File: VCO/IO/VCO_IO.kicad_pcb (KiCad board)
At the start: 2 copper layers, 43.2 x 111.8 mm, 31 parts, among them J1 Saw, J10 Sync, J11 LIN, J12 IO, J2 CV1, J3 CV2, J4 CV3, J5 Pulse, J6 Ramp, J7 Tri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

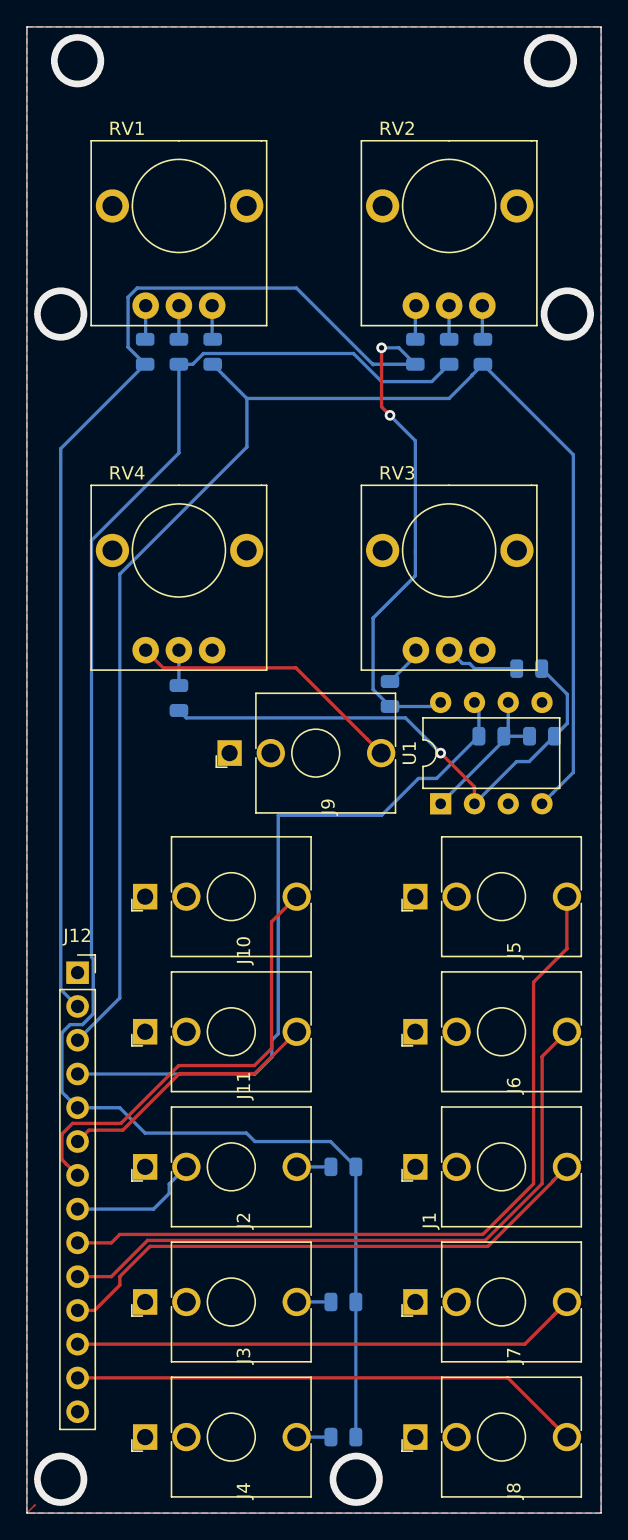
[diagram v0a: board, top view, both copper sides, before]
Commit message: Fix minor issues with VCO board
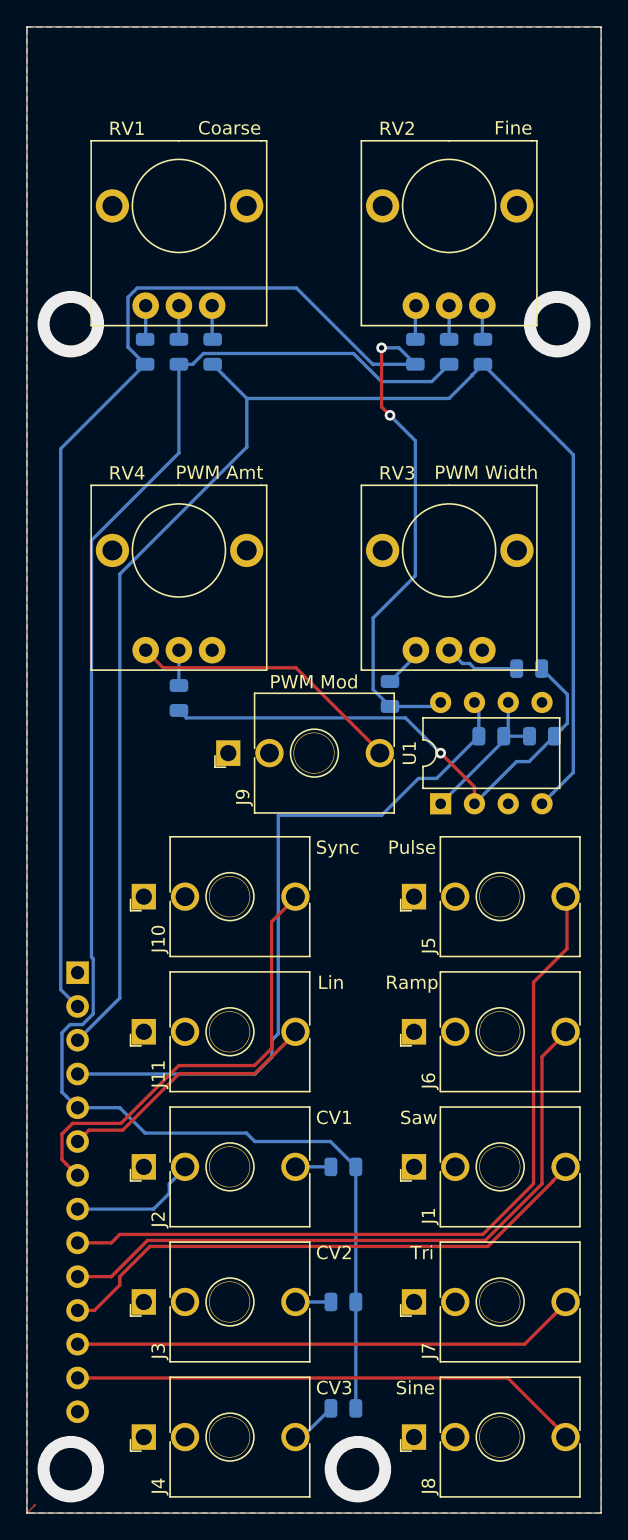
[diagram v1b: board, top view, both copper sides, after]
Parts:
- added REF**: OSHW-Logo2_7.3x6mm_SilkScreen, Symbol:OSHW-Logo2_7.3x6mm_SilkScreen, B.Cu at (77.2, 52.8)
- J12: moved to B.Cu
- moved R7 2.16 mm to (91.1, 152.1)
- turned J12 to 180 degrees
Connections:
- RV1 pad : (no net) -> GNDREF
- RV2 pad : (no net) -> GNDREF
- RV3 pad : (no net) -> GNDREF
- RV4 pad : (no net) -> GNDREF
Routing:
- net /CV: track 125.9 -> 123.7 mm
- net Net-(J4-PadT): track 2.57 -> 3.46 mm
- net GNDREF: vias 6 -> 4
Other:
- board text added: "CV1"
- board text added: "CV2"
- board text added: "CV3"
- board text added: "Coarse"
- board text added: "Fine"
- board text added: "Lin"
- board text added: "PWM Amt"
- board text added: "PWM Mod"
- board text added: "PWM Width"
- board text added: "Pulse"
- board text added: "Ramp"
- board text added: "Saw"
- board text added: "Sine"
- board text added: "Sync"
- board text added: "Tri"
- board text added: "VCO IO Board Rev 1"
- board text added: "WH"

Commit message: Bunch of bug fixes and tweaks
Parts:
- added H1: Top_MH1, Eurorack:eurorack_mounting_hole, F.Cu at (70.6, 70.6)
- added H2: Bottom_MH1, Eurorack:eurorack_mounting_hole, F.Cu at (70.6, 156.7)
- added H3: Top_MH2, Eurorack:eurorack_mounting_hole, F.Cu at (107.2, 70.6)
- added H4: Bottom_MH2, Eurorack:eurorack_mounting_hole, F.Cu at (92.2, 156.7)
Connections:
- RV1 pad : GNDREF -> (no net)
- RV2 pad : GNDREF -> (no net)
- RV3 pad : GNDREF -> (no net)
- RV4 pad : GNDREF -> (no net)
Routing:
- net /PWM: track 53.7 -> 50.6 mm
- net GNDREF: vias 4 -> 0

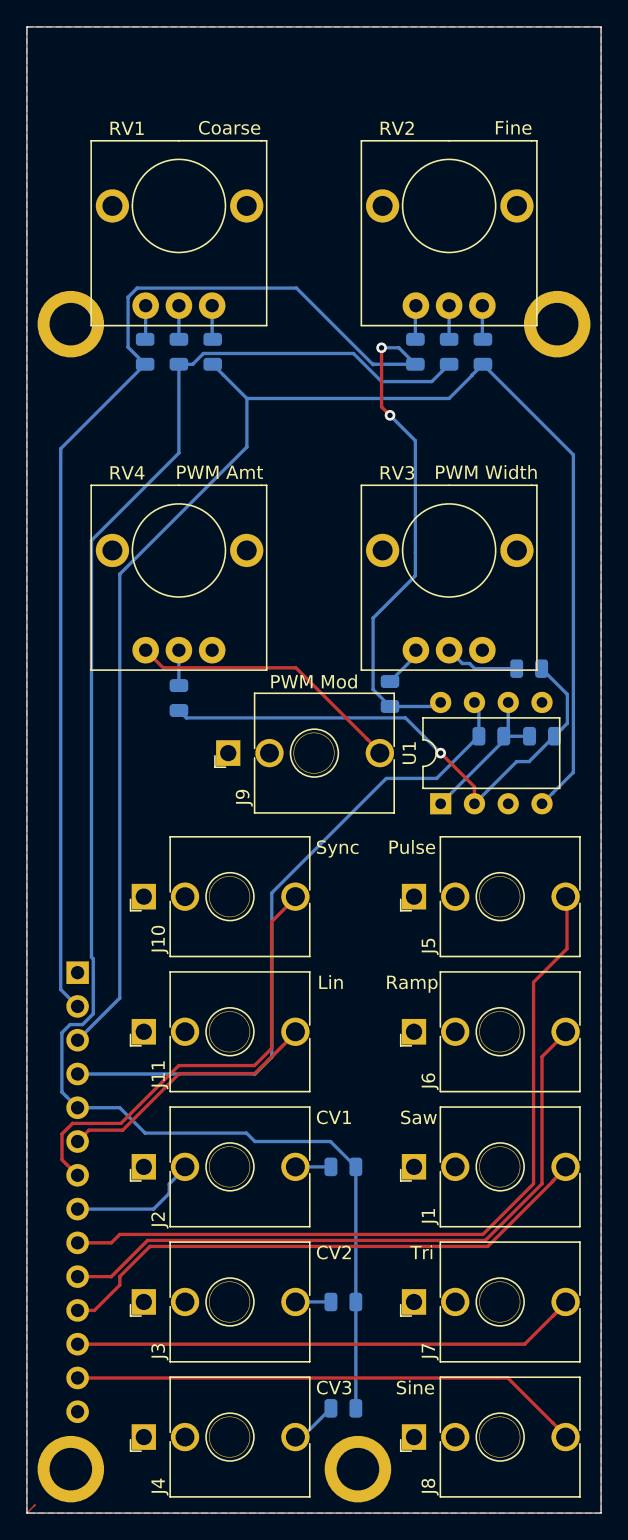
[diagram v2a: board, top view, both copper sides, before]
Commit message: Add resistor divider for Sync input and some capacitors.
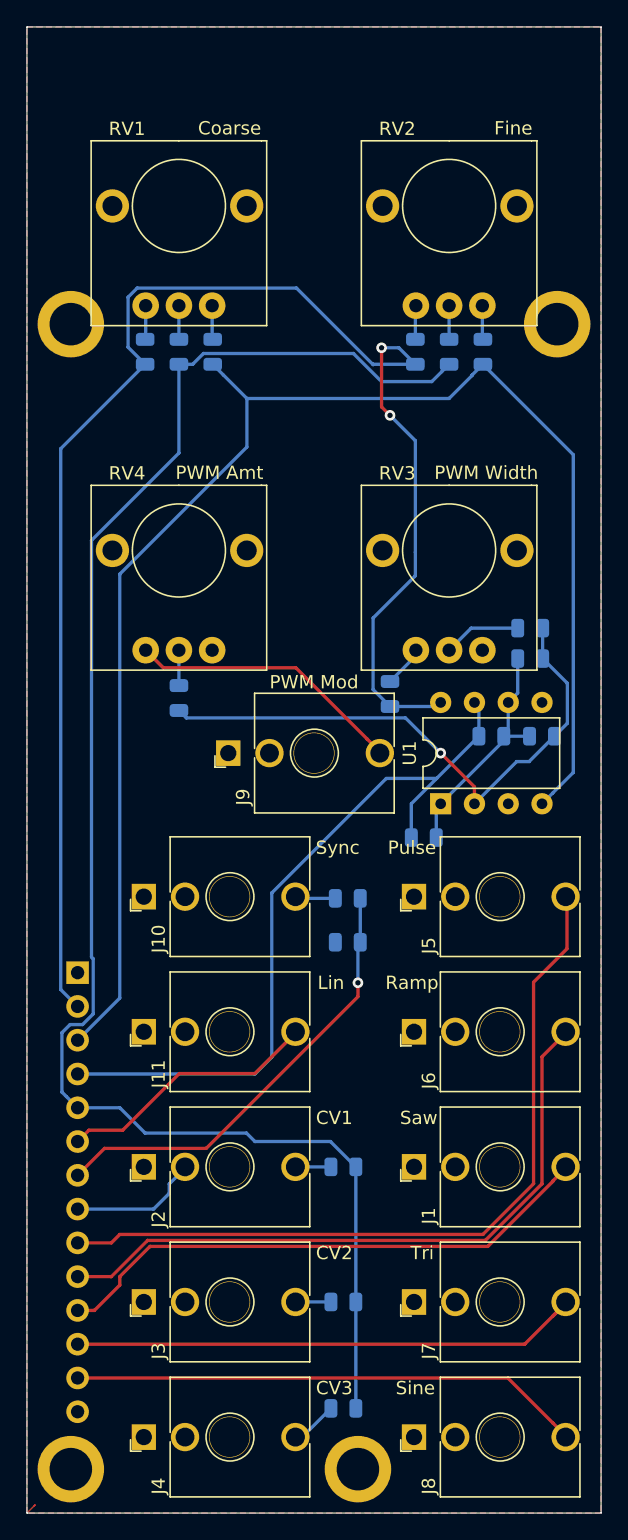
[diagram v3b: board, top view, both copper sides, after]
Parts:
- added C1: C, Capacitor_SMD:C_0805_2012Metric, B.Cu at (105.2, 95.8)
- added C2: C, Capacitor_SMD:C_0805_2012Metric, B.Cu at (97.2, 109.2)
- added R15: 30K, Resistor_SMD:R_0805_2012Metric, B.Cu at (91.4, 113.8)
- added R16: 10K, Resistor_SMD:R_0805_2012Metric, B.Cu at (91.4, 117.1)
- moved R11 3.05 mm to (105.2, 93.5)
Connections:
- J10 pad T: /SYNC -> Net-(J10-PadT)
- RV1 pad : (no net) -> GNDREF
- RV2 pad : (no net) -> GNDREF
- RV3 pad : (no net) -> GNDREF
- RV4 pad : (no net) -> GNDREF
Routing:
- net Net-(C1-Pad1): track 11.7 -> 17.9 mm
- net /PWM: track 50.6 -> 55.8 mm
- net Net-(J10-PadT): track 0.00 -> 3.06 mm
- net Net-(C1-Pad2): track 40.3 -> 43.3 mm
- net /SYNC: track 34.2 -> 34.1 mm, vias 0 -> 1

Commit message: Clean up layout of VCO board
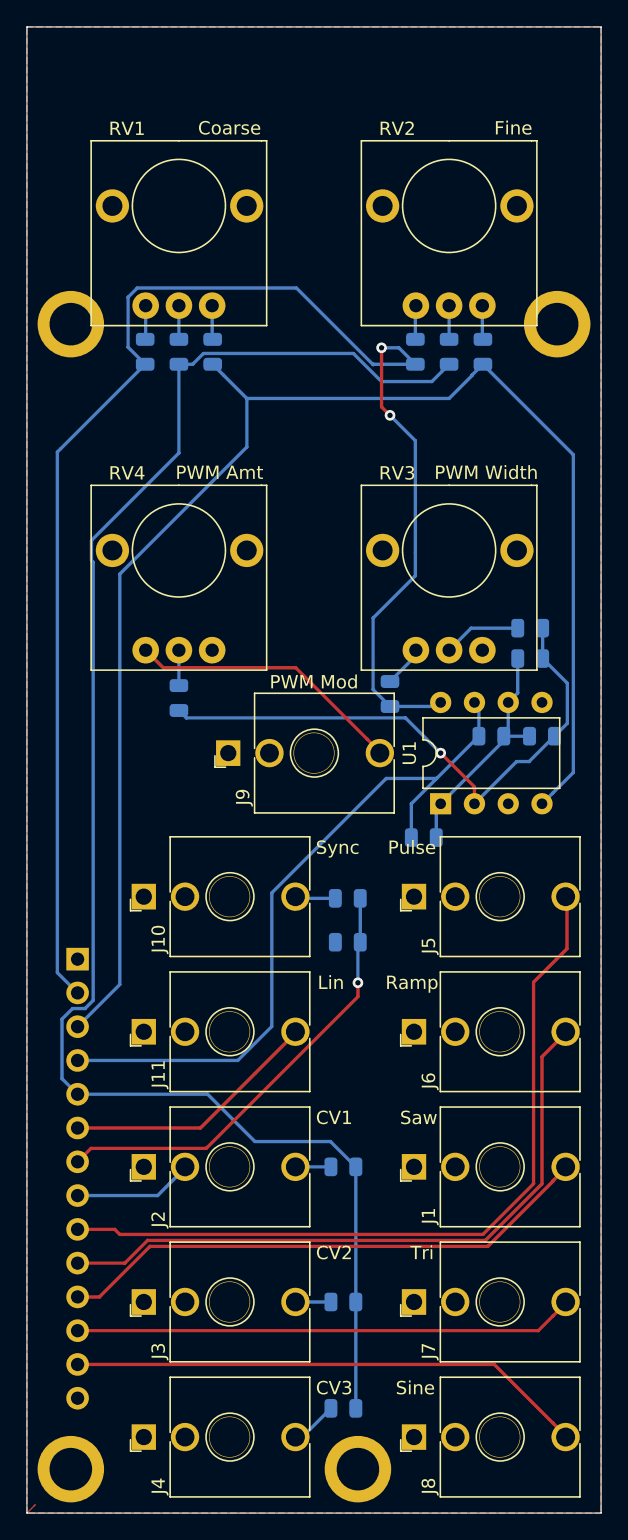
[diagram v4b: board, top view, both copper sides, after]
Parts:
- moved J12 1.02 mm to (71.1, 118.4)
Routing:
- net /Tri: track 39.6 -> 37.7 mm
- net /PWM: track 55.8 -> 54.1 mm
- net -12V: track 112.8 -> 111.8 mm
- net /REAR_CV: track 9.91 -> 9.07 mm
- net +12V: track 118.2 -> 117.4 mm
- net /Saw: track 41.7 -> 40.9 mm
- net /CV: track 123.7 -> 123.1 mm

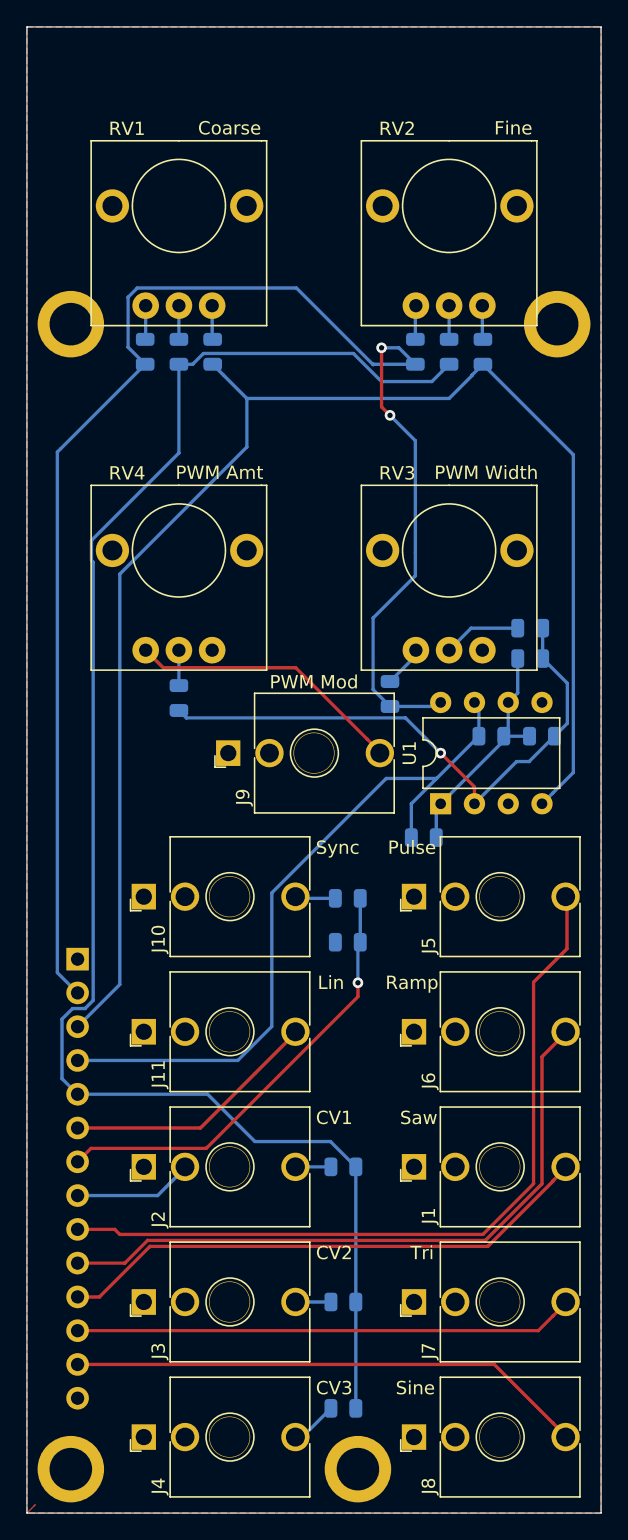
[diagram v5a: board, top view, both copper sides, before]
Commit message: Fix backwards knobs
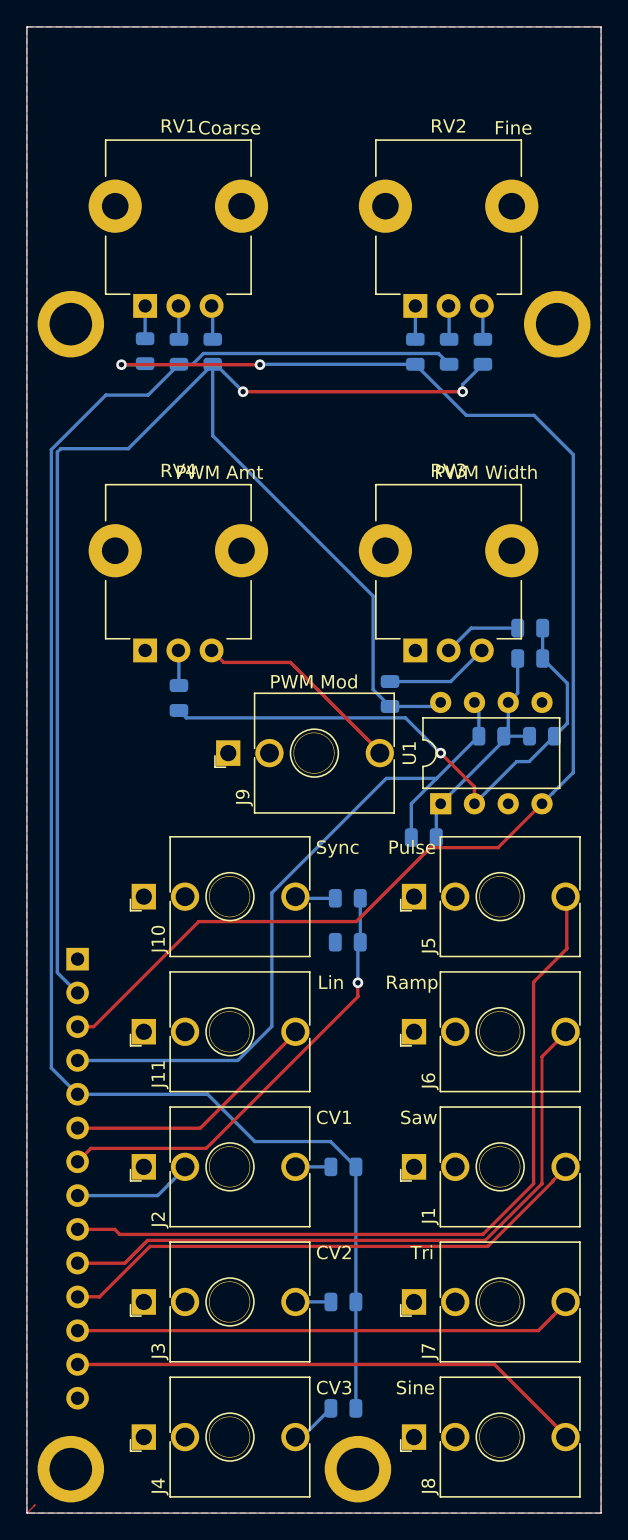
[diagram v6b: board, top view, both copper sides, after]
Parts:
- removed REF**: OSHW-Logo2_7.3x6mm_SilkScreen, Symbol:OSHW-Logo2_7.3x6mm_SilkScreen
- RV1, RV2, RV3, RV4: footprint Eurorack:TT_P0915N -> Eurorack:Potentiometer_TT_P0915N
- moved R2 5.08 mm to (76.2, 72.6)
- moved R1 5.08 mm to (81.3, 72.7)
- moved R3 5.08 mm to (101.6, 72.7)
- moved R4 5.08 mm to (96.5, 72.7)
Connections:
- RV1 pad 1: Net-(R1-Pad2) -> Net-(R2-Pad1)
- RV1 pad 3: Net-(R2-Pad1) -> Net-(R1-Pad2)
- RV2 pad 1: Net-(R3-Pad2) -> Net-(R4-Pad1)
- RV2 pad 3: Net-(R4-Pad1) -> Net-(R3-Pad2)
- RV3 pad 1: Net-(R10-Pad2) -> GNDREF
- RV3 pad 3: GNDREF -> Net-(R10-Pad2)
- RV4 pad 1: Net-(J9-PadT) -> GNDREF
- RV4 pad 3: GNDREF -> Net-(J9-PadT)
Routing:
- net Net-(J9-PadT): track 20.9 -> 16.1 mm
- net Net-(R10-Pad2): track 3.16 -> 7.87 mm
- net -12V: track 111.8 -> 107.7 mm, vias 0 -> 2
- net +12V: track 117.4 -> 113.3 mm
- net /CV: track 123.1 -> 123.9 mm
